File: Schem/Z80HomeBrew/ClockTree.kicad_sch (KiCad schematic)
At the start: 4 parts, among them U3 74HC4040, U9 74HC00, Y1 ECS-2100AX-147.4

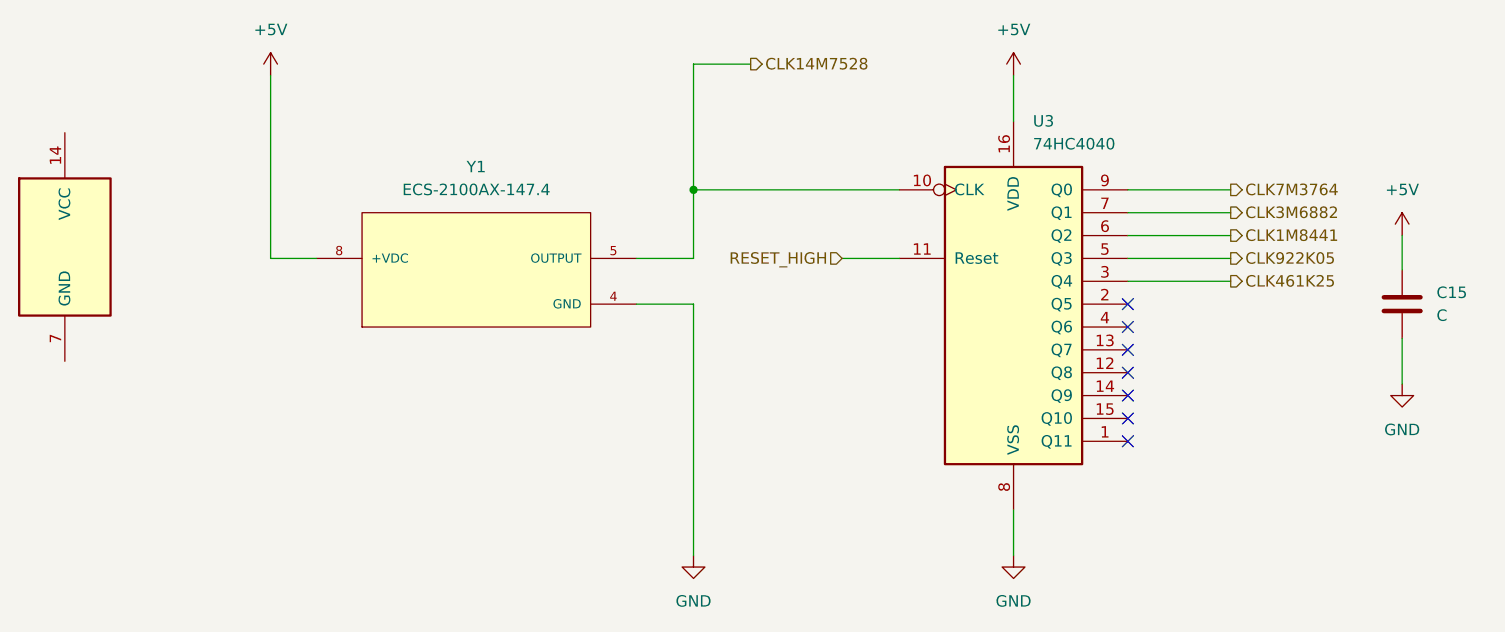
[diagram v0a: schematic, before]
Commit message: Video block added. fixed some issues with parts...
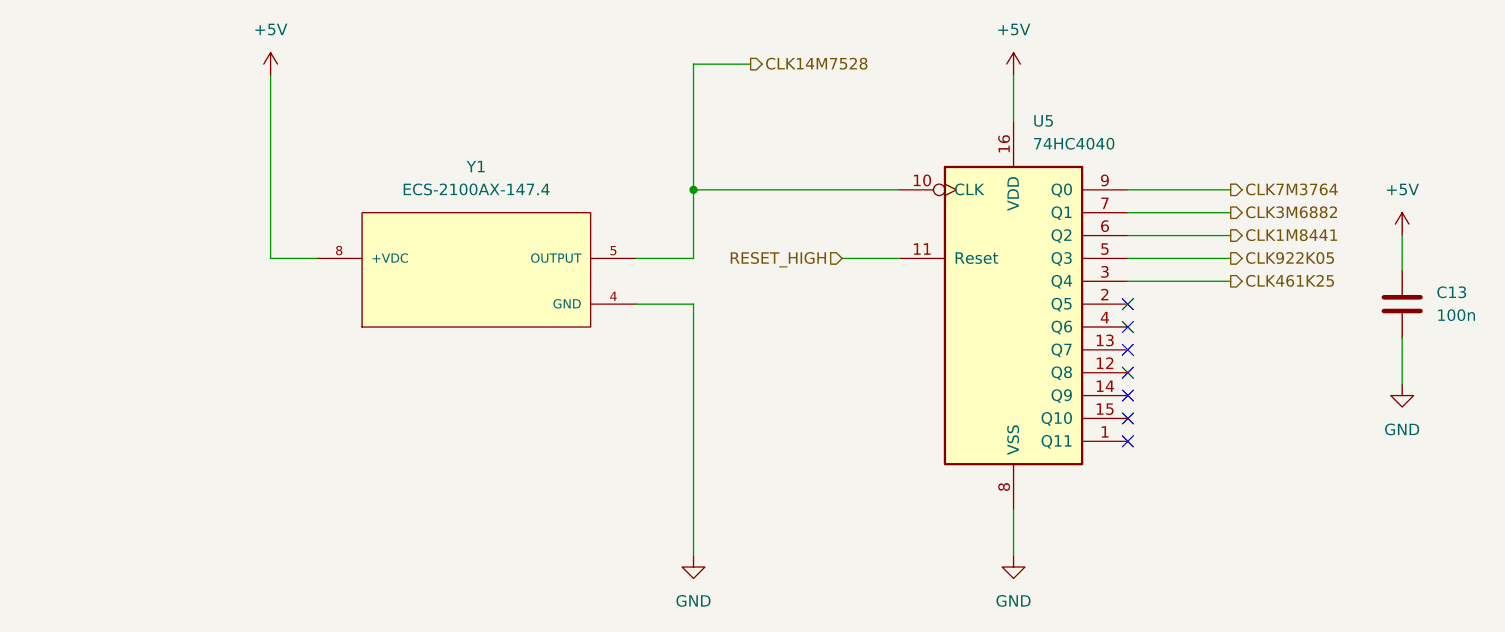
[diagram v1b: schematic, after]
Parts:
- removed U9: 74HC00, symbol 74xx:74HC00
- C13: renamed from C15; value C -> 100n
- renumbered U3 to U5
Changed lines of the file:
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@@
 		(dnp no)
 		(fields_autoplaced yes)
-		(property "Reference" "#PWR038"
+		(property "Reference" "#PWR024"
 			(at 137.16 34.29 0)
 			(effects
@@
 			(project ""
 				(path "/5593e793-d133-45d0-a91e-72805049e474/4d58af3c-6e53-412a-aa45-ebff8f550c35"
-					(reference "#PWR038")
+					(reference "#PWR024")
 					(unit 1)
 				)
@@
 	)
 	(symbol
-		(lib_id "74xx:74HC00")
-		(at 31.75 49.53 0)
-		(unit 5)
-		(exclude_from_sim no)
-		(in_bom yes)
-		(on_board yes)
-		(dnp no)
-		(fields_autoplaced yes)
-		(property "Reference" "U9"
-			(at 38.1 48.2599 0)
-			(effects
-				(font
-					(size 1.27 1.27)
-				)
-				(justify left)
-				(hide yes)
-			)
-		)
-		(property "Value" "74HC00"
-			(at 38.1 50.7999 0)
-			(effects
-				(font
-					(size 1.27 1.27)
-				)
-				(justify left)
-				(hide yes)
-			)
-		)
-		(property "Footprint" ""
-			(at 31.75 49.53 0)
-			(effects
-				(font
-					(size 1.27 1.27)
-				)
-				(hide yes)
-			)
-		)
-		(property "Datasheet" "http://www.ti.com/lit/gpn/sn74hc00"
-			(at 31.75 49.53 0)
-			(effects
-				(font
-					(size 1.27 1.27)
-				)
-				(hide yes)
-			)
-		)
-		(property "Description" "quad 2-input NAND gate"
-			(at 31.75 49.53 0)
-			(effects
-				(font
-					(size 1.27 1.27)
-				)
-				(hide yes)
-			)
-		)
-		(pin "12"
-		)
-		(pin "13"
-		)
-		(pin "9"
-		)
-		(pin "8"
-		)
-		(pin "1"
-		)
-		(pin "5"
-		)
-		(pin "10"
-		)
-		(pin "7"
-		)
-		(pin "11"
-		)
-		(pin "3"
-		)
-		(pin "14"
-		)
-		(pin "4"
-		)
-		(pin "6"
-		)
-		(pin "2"
-		)
-		(instances
-			(project ""
-				(path "/5593e793-d133-45d0-a91e-72805049e474/4d58af3c-6e53-412a-aa45-ebff8f550c35"
-					(reference "U9")
-					(unit 5)
-				)
-			)
-		)
-	)
-	(symbol
 		(lib_id "power:GND")
 		(at 101.6 83.82 0)
@@
 		(dnp no)
 		(fields_autoplaced yes)
-		(property "Reference" "#PWR037"
+		(property "Reference" "#PWR027"
 			(at 101.6 90.17 0)
 			(effects
@@
 			(project "Z80HomeBrew"
 				(path "/5593e793-d133-45d0-a91e-72805049e474/4d58af3c-6e53-412a-aa45-ebff8f550c35"
-					(reference "#PWR037")
+					(reference "#PWR027")
 					(unit 1)
 				)
@@
 		(dnp no)
 		(fields_autoplaced yes)
-		(property "Reference" "#PWR039"
+		(property "Reference" "#PWR023"
 			(at 54.61 34.29 0)
 			(effects
@@
 			(project "Z80HomeBrew"
 				(path "/5593e793-d133-45d0-a91e-72805049e474/4d58af3c-6e53-412a-aa45-ebff8f550c35"
-					(reference "#PWR039")
+					(reference "#PWR023")
 					(unit 1)
 				)
@@
 		(dnp no)
 		(fields_autoplaced yes)
-		(property "Reference" "#PWR041"
+		(property "Reference" "#PWR025"
 			(at 180.34 52.07 0)
 			(effects
@@
 			(project "Z80HomeBrew"
 				(path "/5593e793-d133-45d0-a91e-72805049e474/4d58af3c-6e53-412a-aa45-ebff8f550c35"
-					(reference "#PWR041")
+					(reference "#PWR025")
 					(unit 1)
 				)
@@
 		(dnp no)
 		(fields_autoplaced yes)
-		(property "Reference" "#PWR042"
+		(property "Reference" "#PWR026"
 			(at 180.34 71.12 0)
 			(effects
@@
 			(project "Z80HomeBrew"
 				(path "/5593e793-d133-45d0-a91e-72805049e474/4d58af3c-6e53-412a-aa45-ebff8f550c35"
-					(reference "#PWR042")
+					(reference "#PWR026")
 					(unit 1)
 				)
@@
 		(dnp no)
 		(fields_autoplaced yes)
-		(property "Reference" "#PWR036"
+		(property "Reference" "#PWR028"
 			(at 137.16 90.17 0)
 			(effects
@@
 			(project ""
 				(path "/5593e793-d133-45d0-a91e-72805049e474/4d58af3c-6e53-412a-aa45-ebff8f550c35"
-					(reference "#PWR036")
+					(reference "#PWR028")
 					(unit 1)
 				)
@@
 		(dnp no)
 		(fields_autoplaced yes)
-		(property "Reference" "U3"
+		(property "Reference" "U5"
 			(at 139.3033 35.56 0)
 			(effects
@@
 			(project ""
 				(path "/5593e793-d133-45d0-a91e-72805049e474/4d58af3c-6e53-412a-aa45-ebff8f550c35"
-					(reference "U3")
+					(reference "U5")
 					(unit 1)
 				)
@@
 		(dnp no)
 		(fields_autoplaced yes)
-		(property "Reference" "C15"
+		(property "Reference" "C13"
 			(at 184.15 54.6099 0)
 			(effects
@@
 			)
 		)
-		(property "Value" "C"
+		(property "Value" "100n"
 			(at 184.15 57.1499 0)
 			(effects
@@
 			(project ""
 				(path "/5593e793-d133-45d0-a91e-72805049e474/4d58af3c-6e53-412a-aa45-ebff8f550c35"
-					(reference "C15")
-					(unit 1)
-				)
+					(reference "C13")
+					(unit 1)
+				)

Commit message: Completed schematics
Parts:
- U5: value 74HC4040 -> SN74HC4040DR; footprint Package_SO:SOIC-16W_5.3x10.2mm_P1.27mm -> Package_SO:SO-16_3.9x9.9mm_P1.27mm
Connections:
- net CLK461K25: no longer names the net of U5.3 (Q4)
- net CLK922K05: no longer names the net of U5.5 (Q3)
- no-connect marks 7 -> 9
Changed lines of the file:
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@@
+	)
+	(no_connect
+		(at 149.86 53.34)
 	)
 	(no_connect
@@
 	)
 	(no_connect
+		(at 149.86 50.8)
+	)
+	(no_connect
 		(at 149.86 55.88)
 	)
@@
 	(wire
 		(pts
-			(xy 149.86 53.34) (xy 161.29 53.34)
-		)
-		(stroke
-			(width 0)
-			(type default)
-		)
-	)
-	(wire
-		(pts
 			(xy 101.6 55.88) (xy 101.6 83.82)
 		)
@@
 		(pts
 			(xy 124.46 50.8) (xy 118.11 50.8)
-		)
-		(stroke
-			(width 0)
-			(type default)
-		)
-	)
-	(wire
-		(pts
-			(xy 149.86 50.8) (xy 161.29 50.8)
 		)
 		(stroke
@@
 		)
 	)
-	(hierarchical_label "CLK922K05"
-		(shape output)
-		(at 161.29 50.8 0)
-		(effects
-			(font
-				(size 1.27 1.27)
-			)
-			(justify left)
-		)
-	)
 	(hierarchical_label "RESET_HIGH"
 		(shape input)
@@
 			)
 			(justify right)
-		)
-	)
-	(hierarchical_label "CLK461K25"
-		(shape output)
-		(at 161.29 53.34 0)
-		(effects
-			(font
-				(size 1.27 1.27)
-			)
-			(justify left)
 		)
 	)
@@
 			)
 		)
-		(property "Value" "74HC4040"
+		(property "Value" "SN74HC4040DR"
 			(at 139.3033 38.1 0)
 			(effects
@@
 			)
 		)
-		(property "Footprint" "Package_SO:SOIC-16W_5.3x10.2mm_P1.27mm"
+		(property "Footprint" "Package_SO:SO-16_3.9x9.9mm_P1.27mm"
 			(at 137.16 55.88 0)
 			(effects

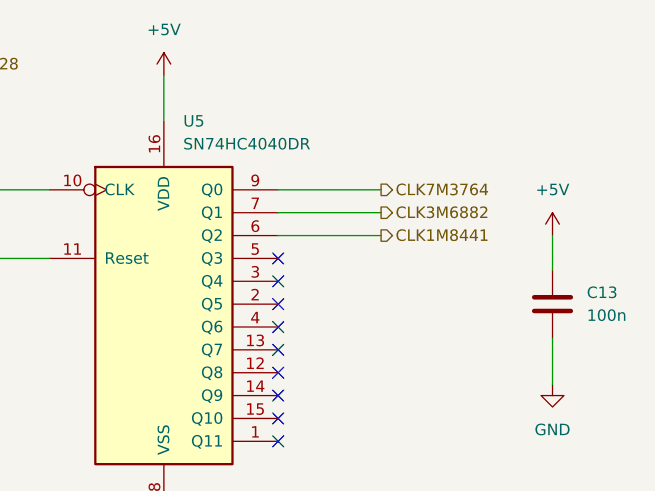
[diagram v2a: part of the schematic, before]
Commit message: Added pBITzBackplane and MezzanineConnector
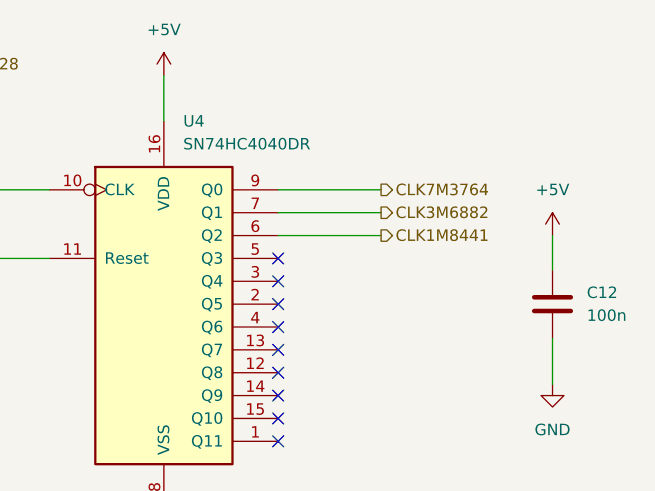
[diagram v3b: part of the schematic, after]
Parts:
- C12: renamed from C13; MANUFACTURER_PART_NUMBER (none) -> C0603C104K5RACTU
- U4: renamed from U5; MANUFACTURER_PART_NUMBER (none) -> SN74HC4040DR
- Y1: MANUFACTURER_PART_NUMBER (none) -> ECS-2100AX-147.4
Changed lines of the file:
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@@
 		(dnp no)
 		(fields_autoplaced yes)
-		(property "Reference" "#PWR024"
+		(property "Reference" "#PWR033"
 			(at 137.16 34.29 0)
 			(effects
@@
 			(project ""
 				(path "/5593e793-d133-45d0-a91e-72805049e474/4d58af3c-6e53-412a-aa45-ebff8f550c35"
-					(reference "#PWR024")
+					(reference "#PWR033")
 					(unit 1)
 				)
@@
 			)
 		)
+		(property "KLC_S4.2_3V3OUT" ""
+			(at 77.47 50.8 0)
+			(effects
+				(font
+					(size 1.27 1.27)
+				)
+				(hide yes)
+			)
+		)
+		(property "KLC_S4.2_VCC" ""
+			(at 77.47 50.8 0)
+			(effects
+				(font
+					(size 1.27 1.27)
+				)
+				(hide yes)
+			)
+		)
+		(property "MANUFACTURER_PART_NUMBER" "ECS-2100AX-147.4"
+			(at 77.47 50.8 0)
+			(effects
+				(font
+					(size 1.27 1.27)
+				)
+				(hide yes)
+			)
+		)
 		(pin "5"
 		)
@@
 		(dnp no)
 		(fields_autoplaced yes)
-		(property "Reference" "#PWR027"
+		(property "Reference" "#PWR036"
 			(at 101.6 90.17 0)
 			(effects
@@
 			(project "Z80HomeBrew"
 				(path "/5593e793-d133-45d0-a91e-72805049e474/4d58af3c-6e53-412a-aa45-ebff8f550c35"
-					(reference "#PWR027")
+					(reference "#PWR036")
 					(unit 1)
 				)
@@
 		(dnp no)
 		(fields_autoplaced yes)
-		(property "Reference" "#PWR023"
+		(property "Reference" "#PWR032"
 			(at 54.61 34.29 0)
 			(effects
@@
 			(project "Z80HomeBrew"
 				(path "/5593e793-d133-45d0-a91e-72805049e474/4d58af3c-6e53-412a-aa45-ebff8f550c35"
-					(reference "#PWR023")
+					(reference "#PWR032")
 					(unit 1)
 				)
@@
 		(dnp no)
 		(fields_autoplaced yes)
-		(property "Reference" "#PWR025"
+		(property "Reference" "#PWR034"
 			(at 180.34 52.07 0)
 			(effects
@@
 			(project "Z80HomeBrew"
 				(path "/5593e793-d133-45d0-a91e-72805049e474/4d58af3c-6e53-412a-aa45-ebff8f550c35"
-					(reference "#PWR025")
+					(reference "#PWR034")
 					(unit 1)
 				)
@@
 		(dnp no)
 		(fields_autoplaced yes)
-		(property "Reference" "#PWR026"
+		(property "Reference" "#PWR035"
 			(at 180.34 71.12 0)
 			(effects
@@
 			(project "Z80HomeBrew"
 				(path "/5593e793-d133-45d0-a91e-72805049e474/4d58af3c-6e53-412a-aa45-ebff8f550c35"
-					(reference "#PWR026")
+					(reference "#PWR035")
 					(unit 1)
 				)
@@
 		(dnp no)
 		(fields_autoplaced yes)
-		(property "Reference" "#PWR028"
+		(property "Reference" "#PWR037"
 			(at 137.16 90.17 0)
 			(effects
@@
 			(project ""
 				(path "/5593e793-d133-45d0-a91e-72805049e474/4d58af3c-6e53-412a-aa45-ebff8f550c35"
-					(reference "#PWR028")
+					(reference "#PWR037")
 					(unit 1)
 				)
@@
 		(dnp no)
 		(fields_autoplaced yes)
-		(property "Reference" "U5"
+		(property "Reference" "U4"
 			(at 139.3033 35.56 0)
 			(effects
@@
 			)
 		)
+		(property "KLC_S4.2_3V3OUT" ""
+			(at 137.16 55.88 0)
+			(effects
+				(font
+					(size 1.27 1.27)
+				)
+				(hide yes)
+			)
+		)
+		(property "KLC_S4.2_VCC" ""
+			(at 137.16 55.88 0)
+			(effects
+				(font
+					(size 1.27 1.27)
+				)
+				(hide yes)
+			)
+		)
+		(property "MANUFACTURER_PART_NUMBER" "SN74HC4040DR"
+			(at 137.16 55.88 0)
+			(effects
+				(font
+					(size 1.27 1.27)
+				)
+				(hide yes)
+			)
+		)
 		(pin "12"
 		)
@@
 			(project ""
 				(path "/5593e793-d133-45d0-a91e-72805049e474/4d58af3c-6e53-412a-aa45-ebff8f550c35"
-					(reference "U5")
+					(reference "U4")
 					(unit 1)
 				)
@@
 		(dnp no)
 		(fields_autoplaced yes)
-		(property "Reference" "C13"
+		(property "Reference" "C12"
 			(at 184.15 54.6099 0)
 			(effects
@@
 			)
 		)
+		(property "KLC_S4.2_3V3OUT" ""
+			(at 180.34 55.88 0)
+			(effects
+				(font
+					(size 1.27 1.27)
+				)
+				(hide yes)
+			)
+		)
+		(property "KLC_S4.2_VCC" ""
+			(at 180.34 55.88 0)
+			(effects
+				(font
+					(size 1.27 1.27)
+				)
+				(hide yes)
+			)
+		)
+		(property "MANUFACTURER_PART_NUMBER" "C0603C104K5RACTU"
+			(at 180.34 55.88 0)
+			(effects
+				(font
+					(size 1.27 1.27)
+				)
+				(hide yes)
+			)
+		)
 		(pin "1"
 		)
@@
 			(project ""
 				(path "/5593e793-d133-45d0-a91e-72805049e474/4d58af3c-6e53-412a-aa45-ebff8f550c35"
-					(reference "C13")
-					(unit 1)
-				)
+					(reference "C12")
+					(unit 1)
+				)
